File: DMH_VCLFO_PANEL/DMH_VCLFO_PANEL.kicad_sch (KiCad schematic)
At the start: 5 parts, among them J0 Panel_GND_Solder_Wire_Pad

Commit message: V1 one the panel ready
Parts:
- added H10, H23, H33: Sine, SynthStuff:Jack_6.35mm_Cutout_Output_v6, symbol SynthStuff:MountingHole_Jack6.35mm_Output_v2
- added H11, H24, H34: Random, SynthStuff:Jack_6.35mm_Cutout_Output_v6, symbol SynthStuff:MountingHole_Jack6.35mm_Output_v2
- added H12, H16, H26: Frequency, SynthStuff:Pot_Cutout_Medium_v2, symbol SynthStuff:MountingHole_Pot
- added H13, H18, H28: CV Amt, SynthStuff:Pot_Cutout_Tiny_attv_P110KH1, symbol SynthStuff:MountingHole_Pot
- added H14, H15, H25, H36, H37, H38: LED A, SynthStuff:MountingHole_LED_3mm, symbol Mechanical:MountingHole
- added H17, H27, H6: Square, SynthStuff:Jack_6.35mm_Cutout_Output_v6, symbol SynthStuff:MountingHole_Jack6.35mm_Output_v2
- added H19, H29, H7: Triangle, SynthStuff:Jack_6.35mm_Cutout_Output_v6, symbol SynthStuff:MountingHole_Jack6.35mm_Output_v2
- added H20, H30, H5: CV, SynthStuff:Jack_6.35mm_Cutout_v3, symbol SynthStuff:MountingHole_Jack6.35mm_v2
- added H21, H31, H35: Attenuvert, SynthStuff:Pot_Cutout_Tiny_attv_P110KH1, symbol SynthStuff:MountingHole_Pot
- added H22, H32, H9: Ramp, SynthStuff:Jack_6.35mm_Cutout_Output_v6, symbol SynthStuff:MountingHole_Jack6.35mm_Output_v2
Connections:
- net GND: now also H10.1, H11.1, H12.1, H13.1, H16.1, H17.1, H18.1, H19.1, H20.1, H21.1, H22.1, H23.1, H24.1, H26.1, H27.1, H28.1, H29.1, H30.1, H31.1, H32.1, H33.1, H34.1, H35.1, H5.1, H6.1, H7.1, H9.1
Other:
- moved on the sheet: H1, H2, H3, H4, J0

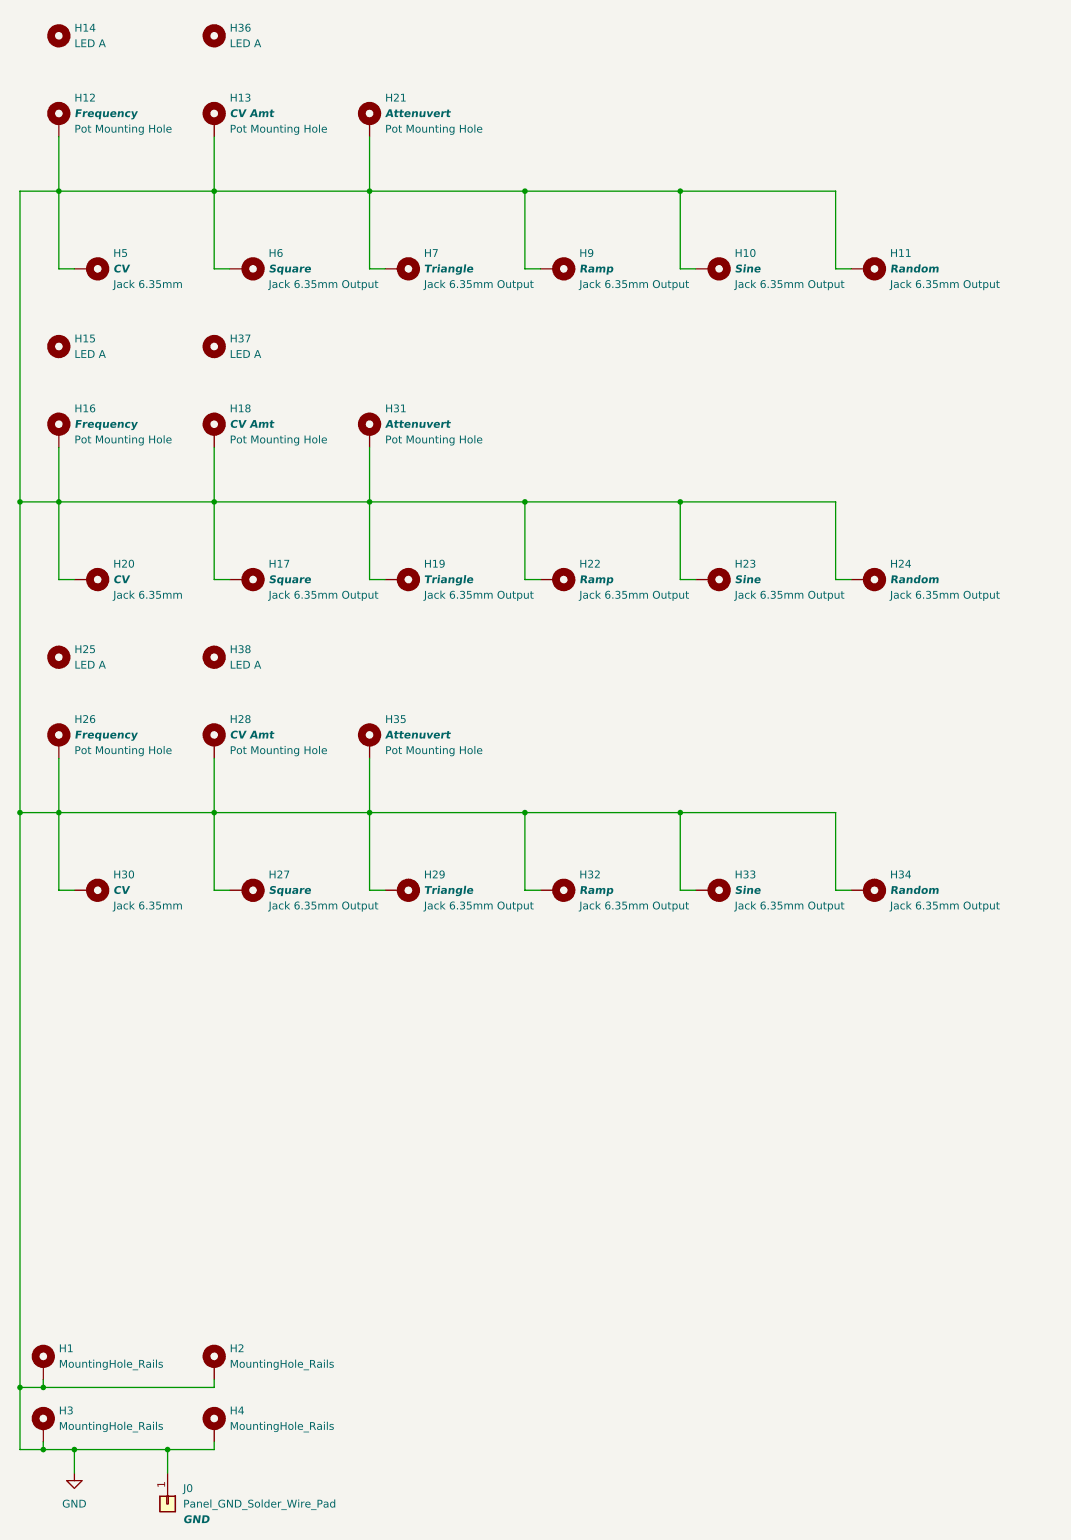
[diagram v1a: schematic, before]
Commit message: V2 panel ready
- Removed attenuverter
- Re-added saw output
- Added sync input
- Added PLL switch
- Added unipolar switch
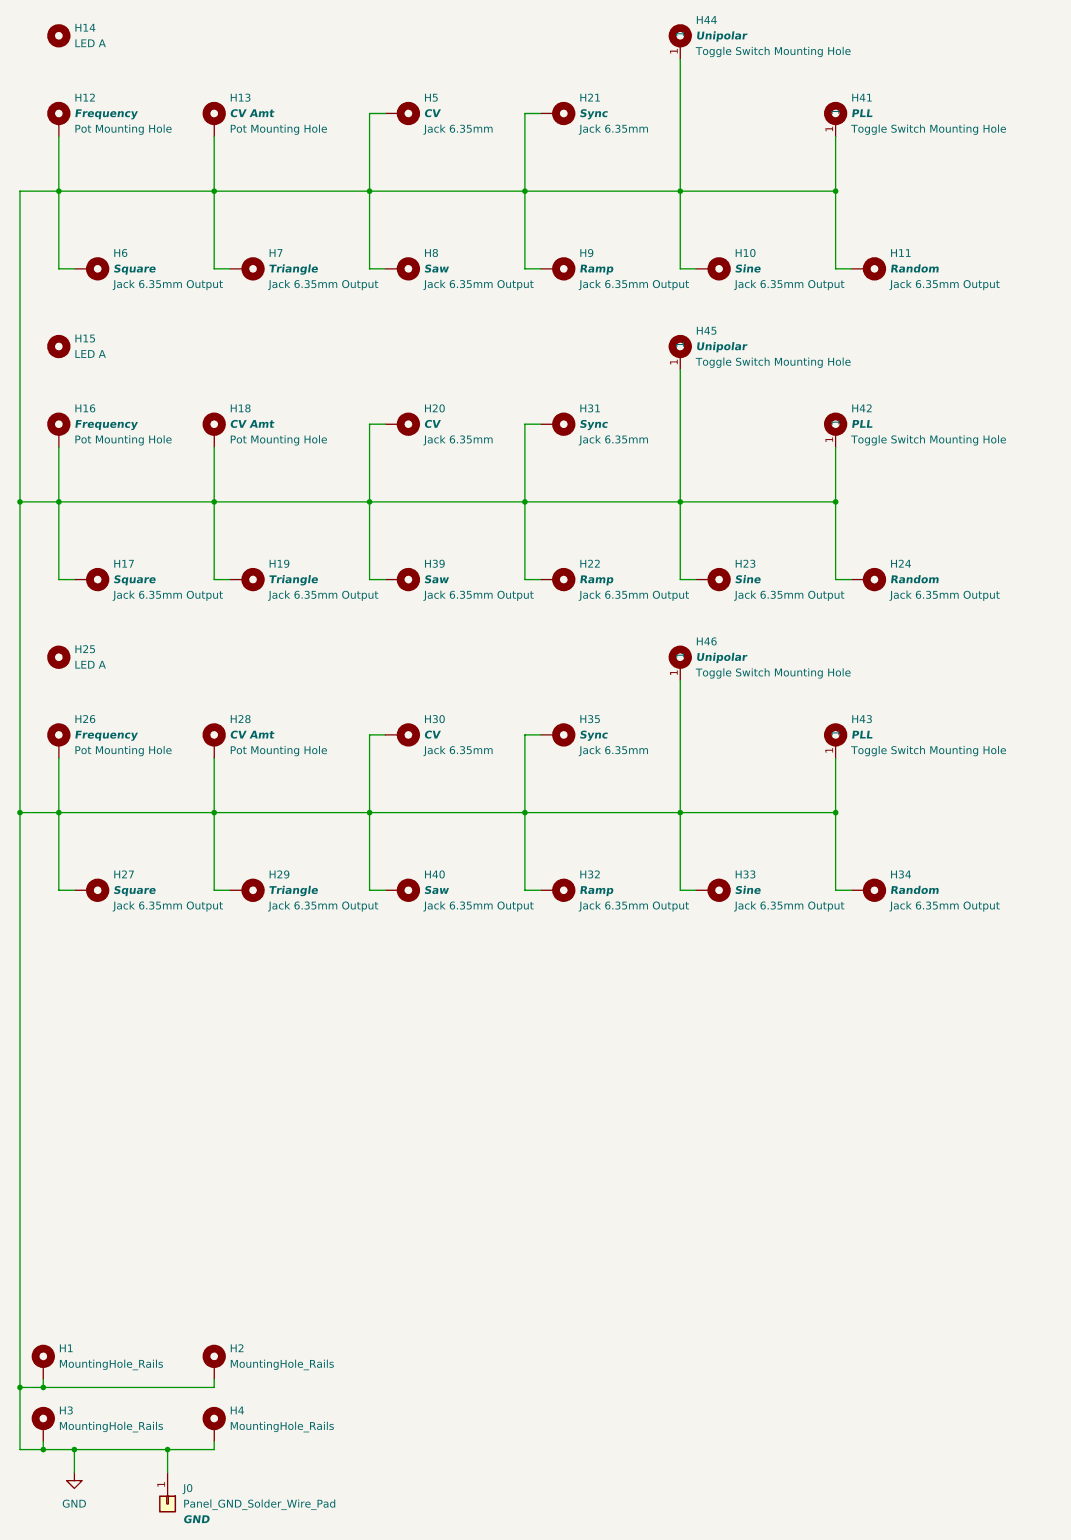
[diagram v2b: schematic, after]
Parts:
- removed H21, H31, H35: Attenuvert, SynthStuff:Pot_Cutout_Tiny_attv_P110KH1, symbol SynthStuff:MountingHole_Pot
- removed H36, H37, H38: LED A, SynthStuff:MountingHole_LED_3mm, symbol Mechanical:MountingHole
- added H21, H31, H35: Sync, SynthStuff:Jack_6.35mm_Cutout_v3, symbol SynthStuff:MountingHole_Jack6.35mm_v2
- added H39, H40, H8: Saw, SynthStuff:Jack_6.35mm_Cutout_Output_v6, symbol SynthStuff:MountingHole_Jack6.35mm_Output_v2
- added H41, H42, H43: PLL, SynthStuff:Toggle_Switch_TE_Cutout, symbol SynthStuff:MountingHole_ToggleSwitch
- added H44, H45, H46: Unipolar, SynthStuff:Toggle_Switch_TE_Cutout, symbol SynthStuff:MountingHole_ToggleSwitch
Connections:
- net GND: now also H21.1, H31.1, H35.1, H39.1, H40.1, H41.1, H42.1, H43.1, H44.1, H45.1, H46.1, H8.1
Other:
- moved on the sheet: H17, H19, H20, H27, H29, H30, H5, H6, H7
